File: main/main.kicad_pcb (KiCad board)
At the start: 2 copper layers, 47 x 35.6 mm, 20 parts, among them J1 AC MAINS, J2 Molex 47054-1000, J5 PROGRAMMING, Q1 MMBT3904, U1 LM7805_TO220, U3 DS18B20, U4 ATtiny5-TS

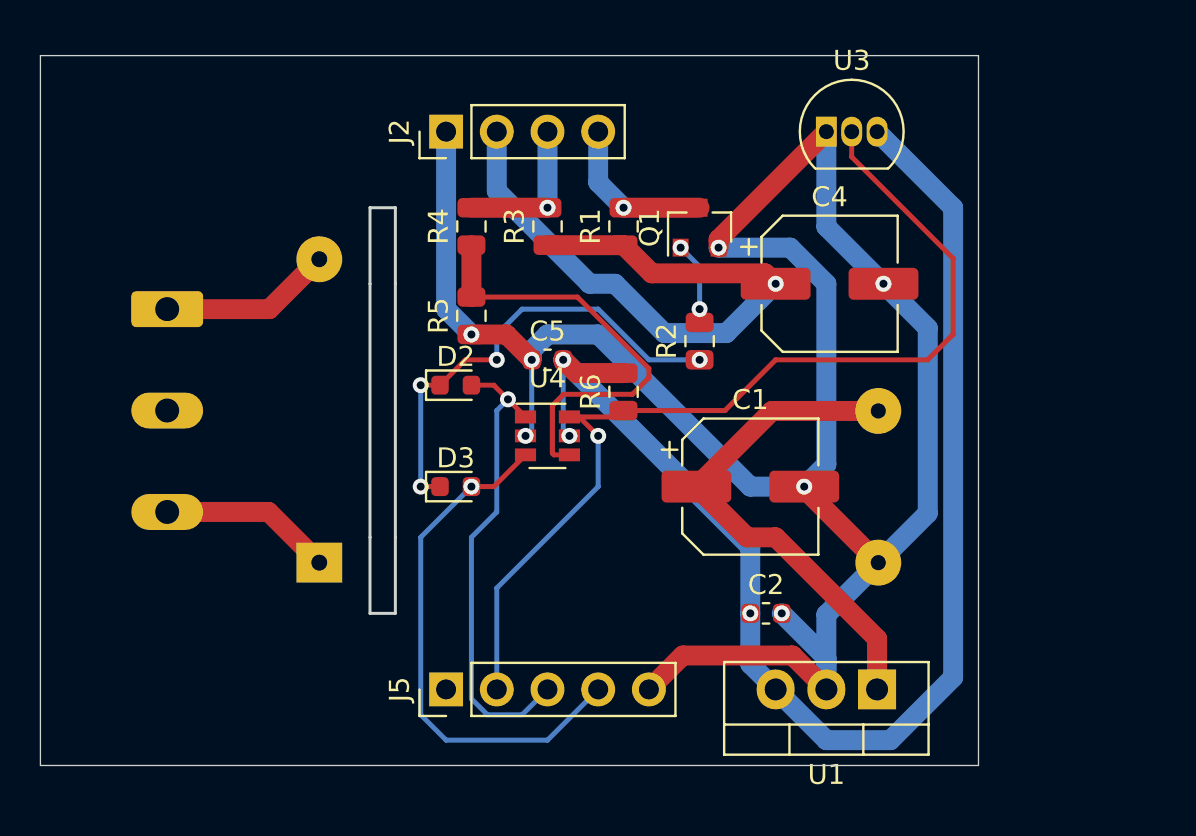
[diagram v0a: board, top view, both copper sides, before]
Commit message: simpler power supply, and slightly better layout
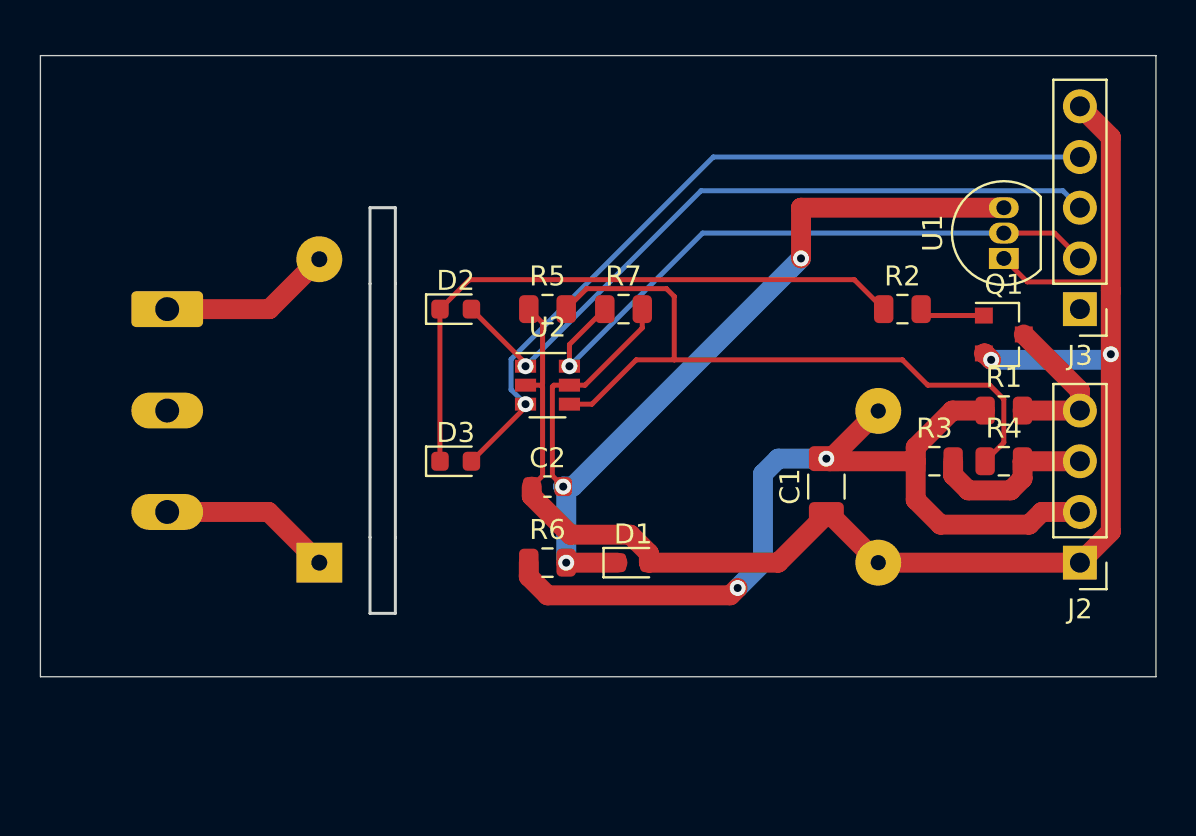
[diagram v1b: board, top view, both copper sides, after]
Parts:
- removed the C2 at (171.0, 119.4)
- removed C4: 10U, Capacitor_SMD:CP_Elec_6.3x5.4_Nichicon
- removed U3: DS18B20, Package_TO_SOT_THT:TO-92_Inline
- added D1: 5V, Diode_SMD:D_0603_1608Metric, F.Cu at (164.3, 116.8)
- added R6: 258/1%, Resistor_SMD:R_0805_2012Metric, F.Cu at (160.0, 116.8)
- C1: value 0U33 -> 10U; footprint Capacitor_SMD:CP_Elec_6.3x5.4_Nichicon -> Capacitor_SMD:C_1206_3216Metric
- U1: value LM7805_TO220 -> DS18B20; footprint Package_TO_SOT_THT:TO-220-3_Vertical -> Package_TO_SOT_THT:TO-92_Inline
- moved J2 38.4 mm to (186.7, 116.8), turned to 180 degrees
- moved J3 37.0 mm to (186.7, 104.1), turned to 180 degrees
- moved R4 29.1 mm to (182.9, 111.8), turned to 0 degrees
- moved R3 22.7 mm to (179.4, 111.8), turned to 0 degrees
- moved U1 22.5 mm to (182.9, 101.6), turned to 90 degrees
- moved R1 21.2 mm to (182.9, 109.2), turned to 0 degrees
- moved Q1 16.2 mm to (182.9, 105.4), turned to 0 degrees
- moved R2 10.3 mm to (177.8, 104.1), turned to 0 degrees
- moved C2 6.35 mm to (160.0, 113.0)
- moved R7 4.14 mm to (163.8, 104.1), turned to 0 degrees
- moved R5 3.82 mm to (160.0, 104.1), turned to 0 degrees
- moved C1 3.81 mm to (174.0, 113.0), turned to 90 degrees
- moved D2 3.81 mm to (155.4, 104.1)
- moved U2 2.54 mm to (160.0, 108.0)
- moved D3 1.27 mm to (155.4, 111.8)
- renumbered C5 to C2, J5 to J3, R6 to R7, U4 to U2
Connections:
- net +5V renamed Net-(C2-Pad2)
- C1 pad 1: Net-(C1-Pad1) -> GND
- C1 pad 2: GND -> +12V
- J3 pad 2: THERMOCOUPLE -> ~RESET
- PS1 pad 4: Net-(C1-Pad1) -> +12V
- R7 pad 1: THERMOCOUPLE -> ~RESET
- U1 pad 1: Net-(C1-Pad1) -> GND
- U1 pad 2: GND -> ~RESET
- U2 pad 6: THERMOCOUPLE -> ~RESET
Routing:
- net THERMOCOUPLE: track 49.4 -> 0.00 mm, vias 1 -> 0
- net GND: track 113.1 -> 78.6 mm, vias 7 -> 2
- net ~RESET: track 0.00 -> 32.5 mm, vias 0 -> 1
- net Net-(C1-Pad1): track 25.4 -> 0.00 mm
- net Net-(C2-Pad2): track 68.3 -> 47.7 mm
- net FAN-TACH: track 22.1 -> 36.2 mm
- net CLOCK: track 26.3 -> 39.2 mm
- net +12V: track 33.1 -> 45.4 mm, vias 1 -> 2
- net DATA: track 23.8 -> 35.7 mm
- net FAN-PWM: track 23.4 -> 31.1 mm, vias 4 -> 0
- net Net-(Q1-Pad1): track 4.14 -> 3.28 mm, vias 2 -> 0
- net TACH: track 7.62 -> 8.48 mm, vias 1 -> 0
- net PWM: track 8.15 -> 7.85 mm, vias 1 -> 0
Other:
- board size 47 x 35.6 mm -> 55.9 x 31.1 mm

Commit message: simpler dumber fan controller, will add pwm feedback and temp sensing later
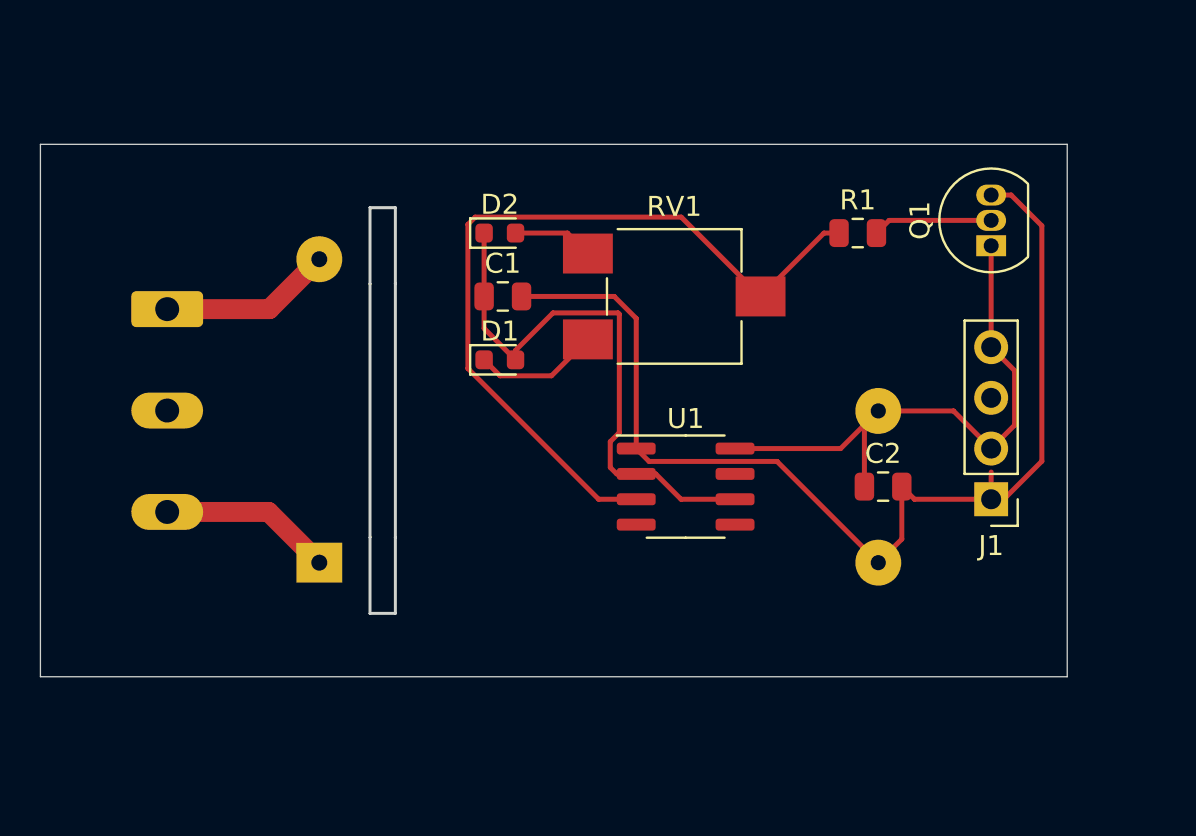
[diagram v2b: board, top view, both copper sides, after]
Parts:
- removed D3: 1N4148, Diode_SMD:D_0603_1608Metric
- removed J3: PROGRAMMING, Connector_PinHeader_2.54mm:PinHeader_1x05_P2.54mm_Vertical
- removed the R1 at (182.9, 109.2)
- removed R3, R7: 4K7/1%, Resistor_SMD:R_0805_2012Metric
- removed R4: 27K4/1%, Resistor_SMD:R_0805_2012Metric
- removed R5: 10K/1%, Resistor_SMD:R_0805_2012Metric
- removed R6: 258/1%, Resistor_SMD:R_0805_2012Metric
- removed U2: ATtiny5-TS, Package_TO_SOT_SMD:SOT-23-6
- added RV1: 10K, Potentiometer_SMD:Potentiometer_ACP_CA6-VSMD_Vertical, F.Cu at (166.4, 103.5)
- C1: value 10U -> 4N7; footprint Capacitor_SMD:C_1206_3216Metric -> Capacitor_SMD:C_0805_2012Metric
- C2: footprint Capacitor_SMD:C_0603_1608Metric -> Capacitor_SMD:C_0805_2012Metric
- D1: value 5V -> 1N4148
- Q1: value MMBT3904 -> BC547; footprint Package_TO_SOT_SMD:SOT-23 -> Package_TO_SOT_THT:TO-92_Inline
- R1: renamed from R2; value 4K7/1% -> 10K
- U1: value DS18B20 -> ICM7555xB; footprint Package_TO_SOT_THT:TO-92_Inline -> Package_SO:SOIC-8_3.9x4.9mm_P1.27mm
- moved U1 19.6 mm to (166.9, 113.0), turned to 0 degrees
- moved C1 18.8 mm to (157.8, 103.5), turned to 0 degrees
- moved C2 16.8 mm to (176.8, 113.0)
- moved D1 12.2 mm to (157.6, 106.7)
- moved J1 5.46 mm to (182.2, 113.7)
- moved Q1 4.49 mm to (182.2, 101.0), turned to 90 degrees
- moved R1 4.42 mm to (175.6, 100.3)
- moved D2 4.40 mm to (157.6, 100.3)
- renumbered J2 to J1, J1 to J2
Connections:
- C1 pad 1: GND -> Net-(C1-Pad1)
- C1 pad 2: +12V -> Net-(C1-Pad2)
- C2 pad 1: GND -> Net-(C2-Pad1)
- C2 pad 2: Net-(C2-Pad2) -> Net-(C1-Pad2)
- D1 pad 1: Net-(C2-Pad2) -> Net-(D1-Pad1)
- D1 pad 2: GND -> Net-(C1-Pad1)
- D2 pad 1: FAN-PWM -> Net-(C1-Pad1)
- D2 pad 2: DATA -> Net-(D2-Pad2)
- J1 pad 1: GND -> Net-(C1-Pad2)
- J1 pad 2: +12V -> Net-(C2-Pad1)
- J1 pad 3: TACH -> (no net)
- J1 pad 4: PWM -> Net-(C2-Pad1)
- PS1 pad 3: GND -> Net-(C1-Pad2)
- PS1 pad 4: +12V -> Net-(C2-Pad1)
- Q1 pad 1: Net-(Q1-Pad1) -> Net-(C2-Pad1)
- Q1 pad 2: GND -> Net-(Q1-Pad2)
- Q1 pad 3: PWM -> Net-(C1-Pad2)
- R1 pad 1: FAN-PWM -> Net-(R1-Pad1)
- R1 pad 2: Net-(Q1-Pad1) -> Net-(Q1-Pad2)
- U1 pad 1: GND -> Net-(C1-Pad2)
- U1 pad 2: ~RESET -> Net-(C1-Pad1)
- U1 pad 3: Net-(C2-Pad2) -> Net-(R1-Pad1)
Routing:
- net GND: track 78.6 -> 0.00 mm, vias 2 -> 0
- net Net-(C1-Pad2): track 0.00 -> 55.9 mm
- net Net-(C2-Pad2): track 47.7 -> 0.00 mm, vias 3 -> 0
- net +12V: track 45.4 -> 0.00 mm, vias 2 -> 0
- net Net-(R1-Pad1): track 0.00 -> 40.1 mm
- net CLOCK: track 39.2 -> 0.00 mm, vias 1 -> 0
- net FAN-TACH: track 36.2 -> 0.00 mm
- net DATA: track 35.7 -> 0.00 mm, vias 1 -> 0
- net ~RESET: track 32.5 -> 0.00 mm, vias 1 -> 0
- net FAN-PWM: track 31.1 -> 0.00 mm
- net Net-(C2-Pad1): track 0.00 -> 29.6 mm
- net Net-(C1-Pad1): track 0.00 -> 28.3 mm
- net TACH: track 8.48 -> 0.00 mm
- net PWM: track 7.85 -> 0.00 mm
- net Net-(D1-Pad1): track 0.00 -> 6.29 mm
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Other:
- board size 55.9 x 31.1 mm -> 51.4 x 26.7 mm
